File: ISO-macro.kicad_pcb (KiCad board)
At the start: 2 copper layers, 105.9 x 38.1 mm, 36 parts, among them J1 USB_C_Receptacle_USB2.0, SW1 SW_SPST, SW2 SW_SPST, SW3 SW_SPST, SW4 SW_SPST, SW5 SW_SPST, SW6 SW_SPST, SW7 SW_SPST, SW8 EC11, SW9 SW_SPST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

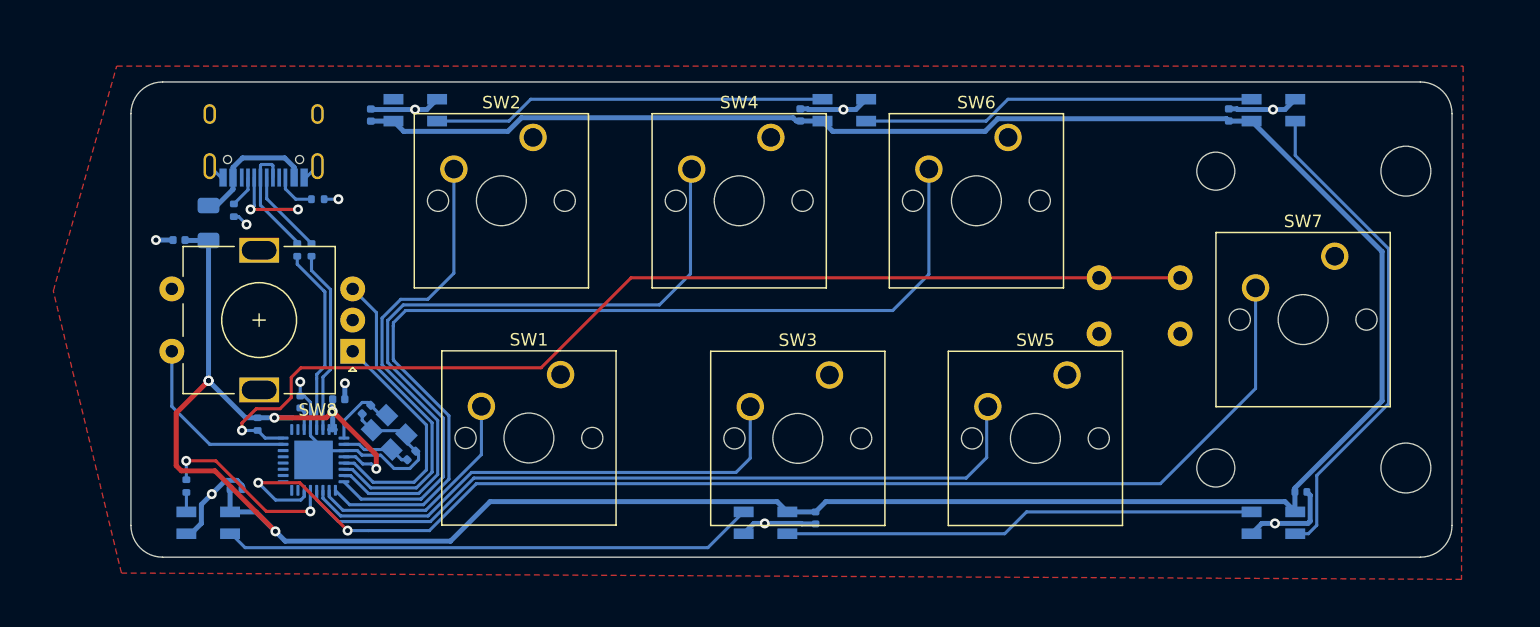
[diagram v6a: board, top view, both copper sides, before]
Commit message: smaller reset footprint, move a few things
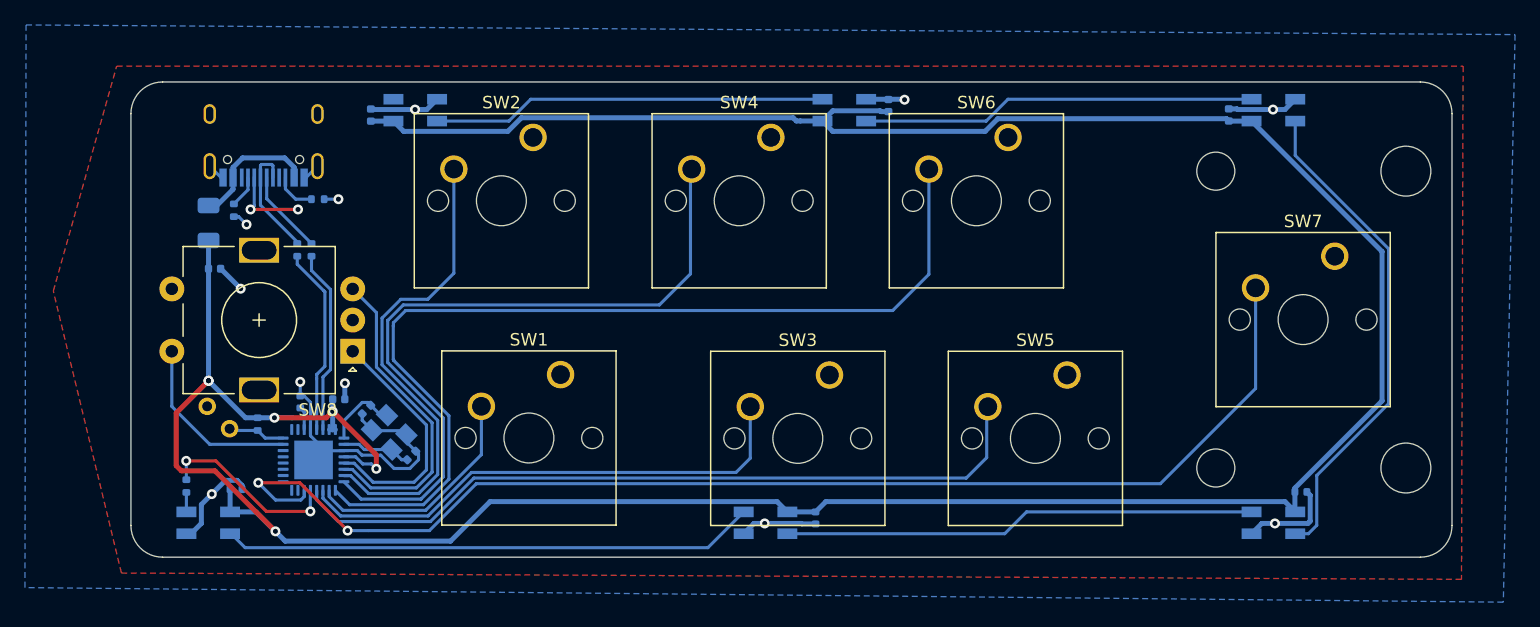
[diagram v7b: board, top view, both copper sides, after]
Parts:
- SW9: footprint Button_Switch_THT:SW_PUSH_6mm -> TestPoint:TestPoint_2Pads_Pitch2.54mm_Drill0.8mm
- moved SW9 77.2 mm to (117.1, 86.1), turned to 135 degrees
- moved C7 7.10 mm to (170.0, 60.2)
- moved C8 3.66 mm to (115.9, 73.3), turned to 0 degrees
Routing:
- net /Reset: track 85.1 -> 4.60 mm, vias 1 -> 0
- net VCC: track 257.4 -> 261.2 mm
- net GND: track 68.1 -> 66.5 mm
- added copper zone on B.Cu, net (none)
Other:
- board text added: "RESET"
